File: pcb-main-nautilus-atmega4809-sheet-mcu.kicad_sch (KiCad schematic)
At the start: 18 parts, among them SW1 PTS645SH43SMTR92 LFS, U4 ATmega4809-A

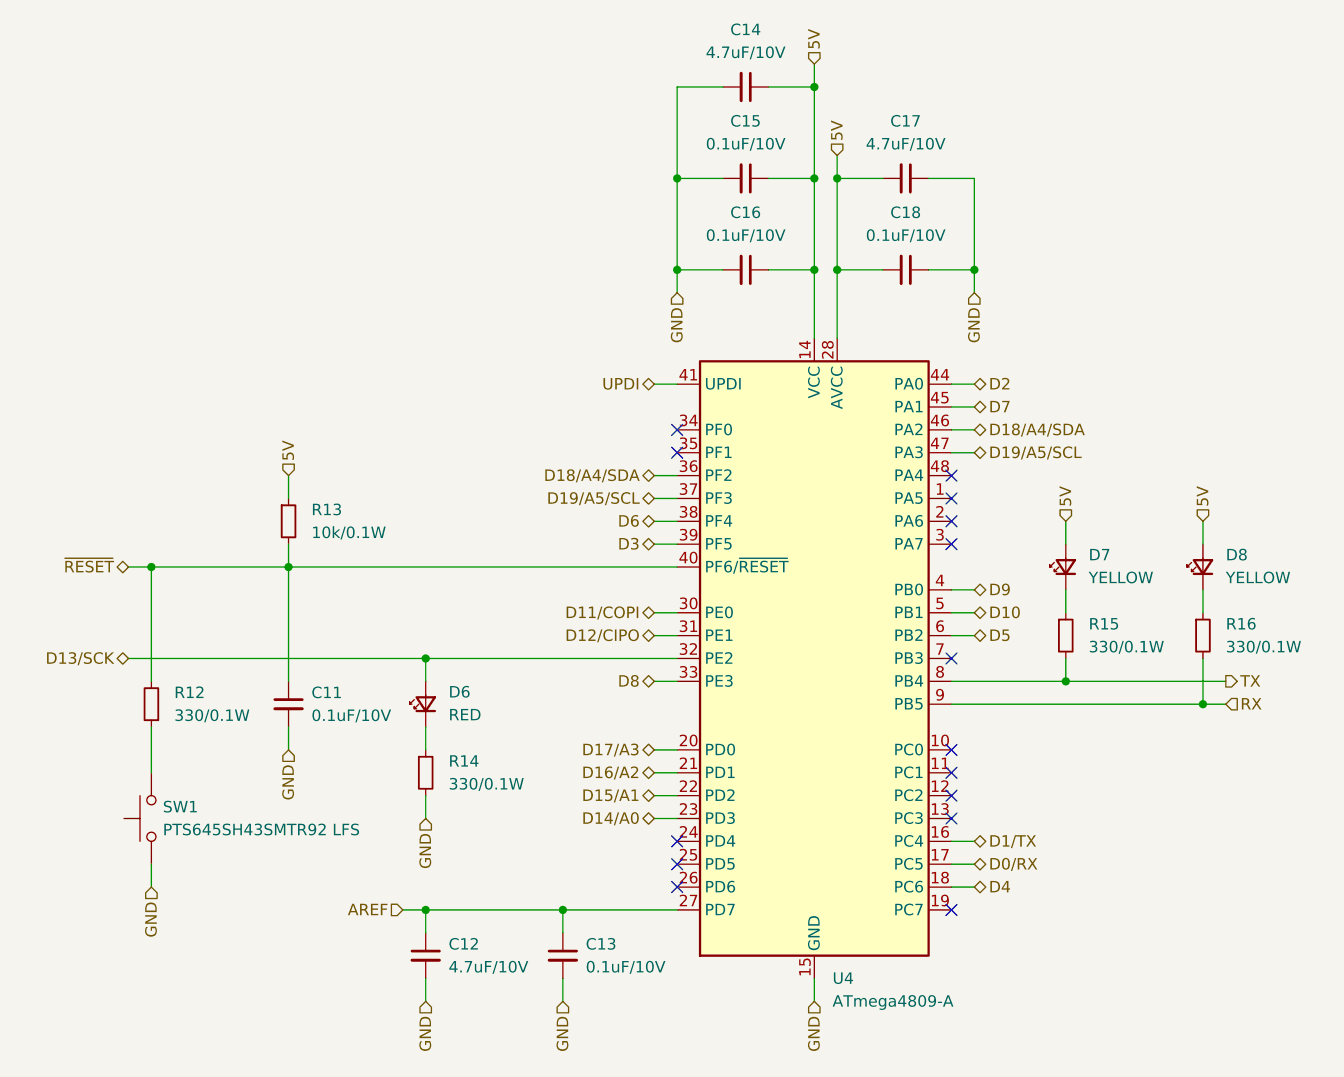
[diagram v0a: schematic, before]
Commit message: Add test points
Supports #2.
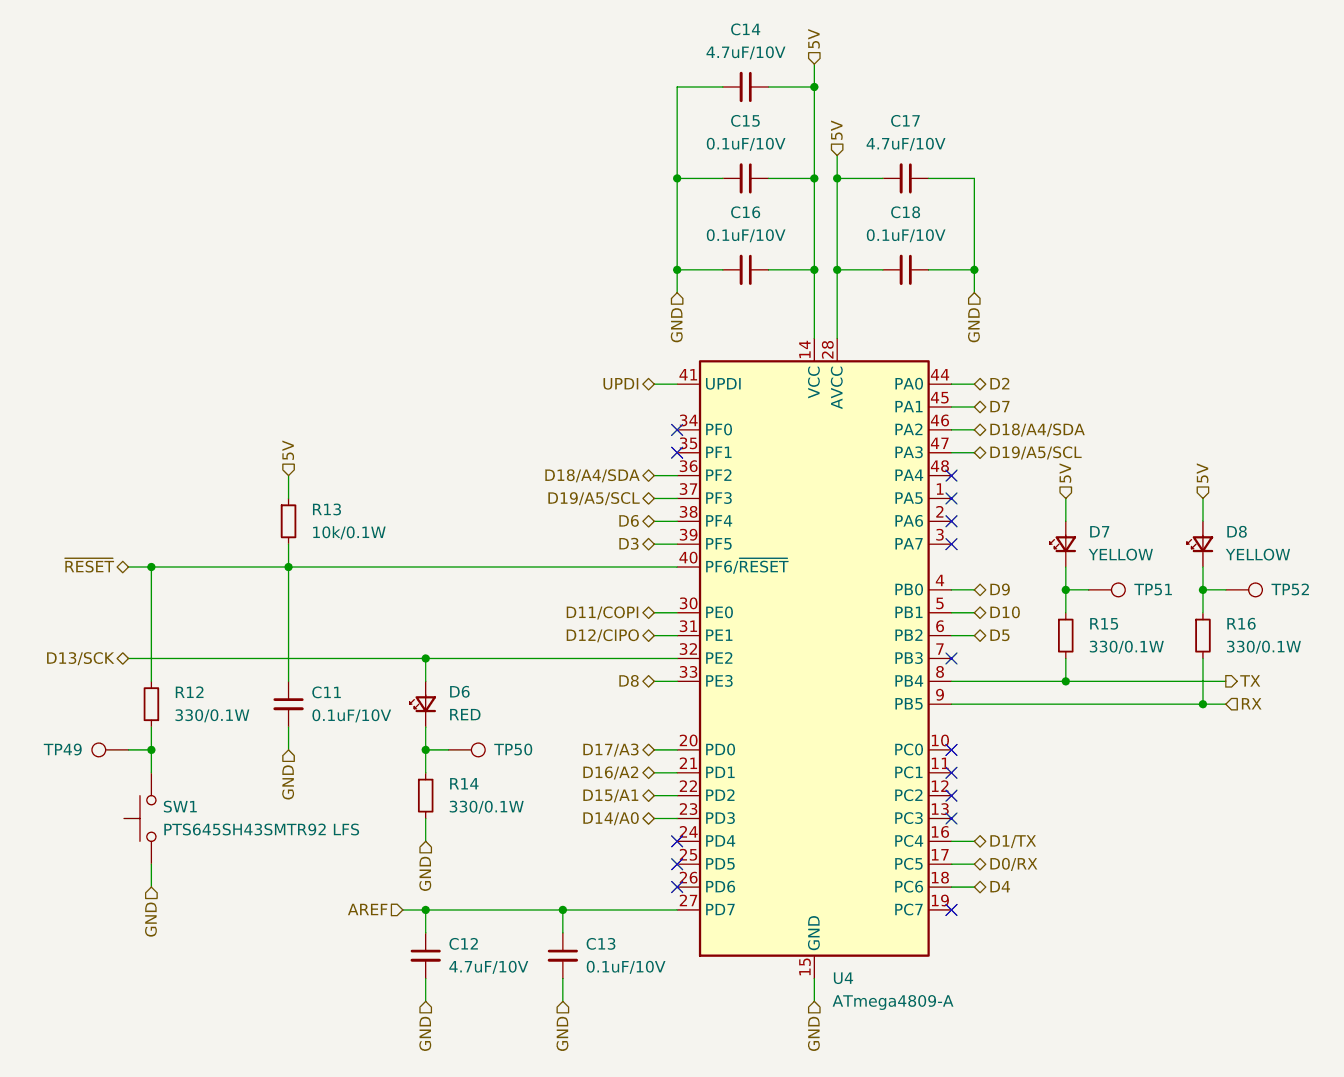
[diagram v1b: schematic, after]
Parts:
- added TP49, TP50, TP51, TP52: TestPoint, TestPoint:TestPoint_Pad_D1.0mm, symbol Connector:TestPoint
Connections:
- net at D6.1 (K), R14.1: now also TP50.1
- net at R12.1, SW1.2: now also TP49.1
- net at D7.1 (K), R15.1: now also TP51.1
- net at D8.1 (K), R16.1: now also TP52.1
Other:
- moved on the sheet: D7, D8, R14

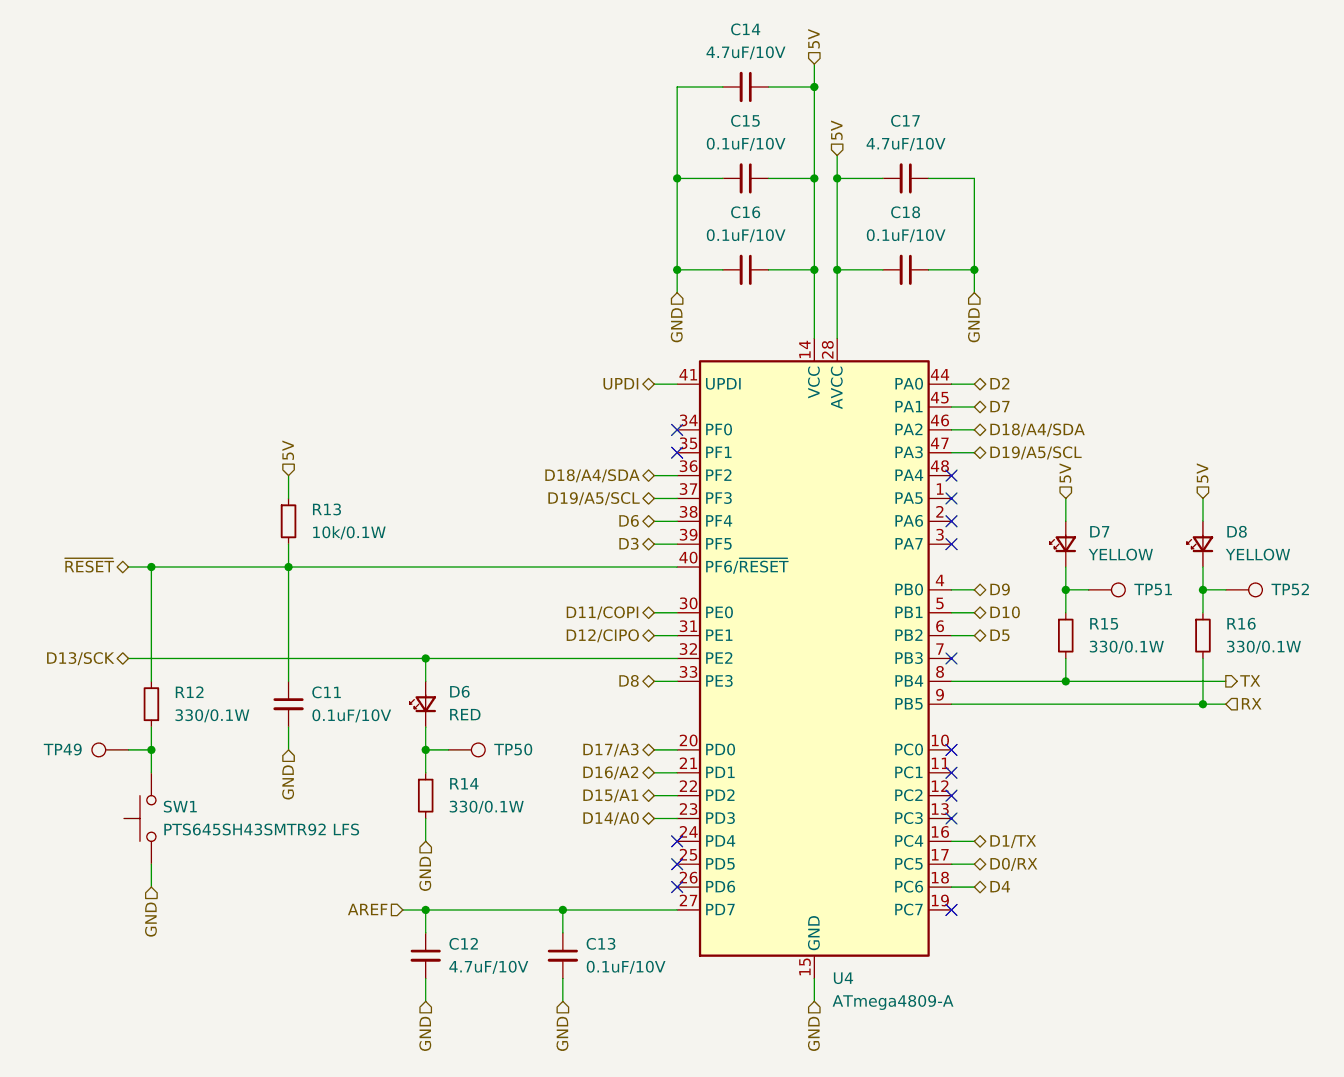
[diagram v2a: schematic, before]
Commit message: Add layout (#4)
Resolves #3 (Add layout).
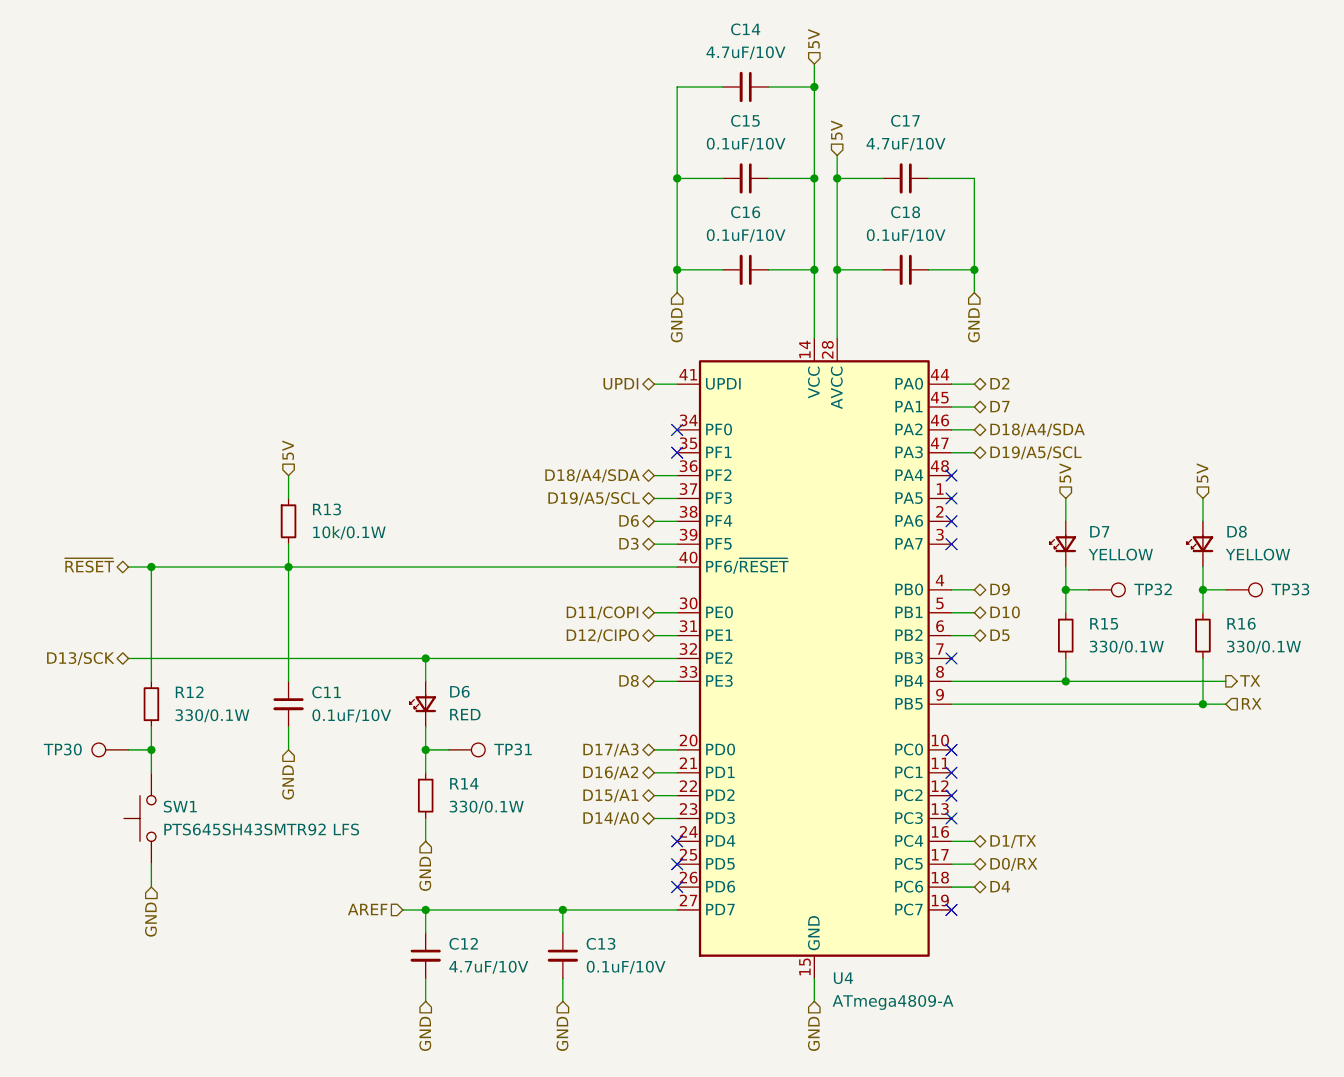
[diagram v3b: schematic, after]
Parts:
- renumbered TP49 to TP30, TP50 to TP31, TP51 to TP32, TP52 to TP33
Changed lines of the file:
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@@
   (symbol (lib_id "Connector:TestPoint") (at 99.06 111.76 270) (unit 1)
     (in_bom yes) (on_board yes)
-    (property "Reference" "TP50" (id 0) (at 104.14 111.76 90)
+    (property "Reference" "TP31" (id 0) (at 104.14 111.76 90)
       (effects (font (size 1.27 1.27)) (justify left))
     )
@@
   (symbol (lib_id "Connector:TestPoint") (at 185.42 93.98 270) (unit 1)
     (in_bom yes) (on_board yes)
-    (property "Reference" "TP52" (id 0) (at 190.5 93.98 90)
+    (property "Reference" "TP33" (id 0) (at 190.5 93.98 90)
       (effects (font (size 1.27 1.27)) (justify left))
     )
@@
   (symbol (lib_id "Connector:TestPoint") (at 170.18 93.98 270) (unit 1)
     (in_bom yes) (on_board yes)
-    (property "Reference" "TP51" (id 0) (at 175.26 93.98 90)
+    (property "Reference" "TP32" (id 0) (at 175.26 93.98 90)
       (effects (font (size 1.27 1.27)) (justify left))
     )
@@
   (symbol (lib_id "Connector:TestPoint") (at 63.5 111.76 90) (unit 1)
     (in_bom yes) (on_board yes)
-    (property "Reference" "TP49" (id 0) (at 58.42 111.76 90)
-      (effects (font (size 1.27 1.27)) (justify left))
-    )
+    (property "Reference" "TP30" (id 0) (at 58.42 111.76 90)
+      (effects (font (size 1.27 1.27)) (justify left))
+    )
